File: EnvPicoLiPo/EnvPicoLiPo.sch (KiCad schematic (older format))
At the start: 72 parts, among them J2 SKRKAEE020, J3 2.54mm header 01x20, J4 2.54mm header 01x20, J5 Conn_01x03_Male, U1 LM3671MF 3.3, U2 BQ24072RGT, U3 RP2040, U4 ESP32-PICO-D4, X1 XO 32 12Mhz 3225 seiko

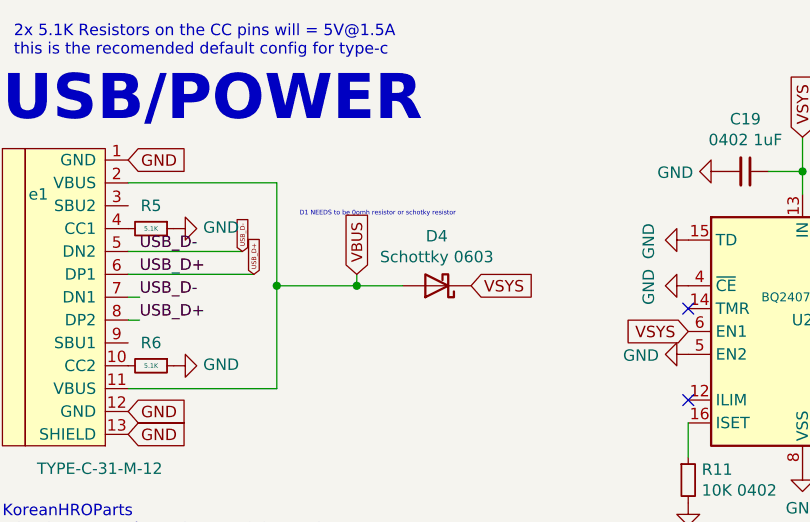
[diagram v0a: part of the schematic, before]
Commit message: Corrected all the via placements so they dont cause issues and removed some redundant parts
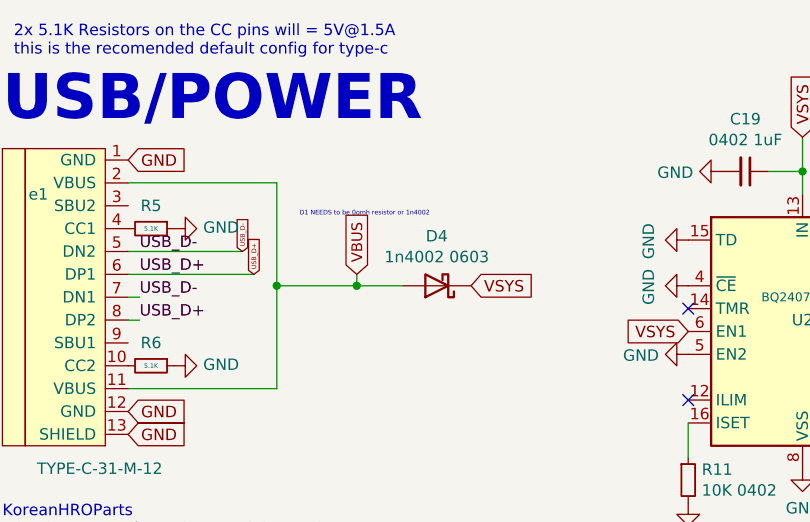
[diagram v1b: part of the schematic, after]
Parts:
- D4: value Schottky 0603 -> 1n4002 0603
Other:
- note added: "D1 NEEDS to be 0omh resistor or 1n4002"
- note removed: "D1 NEEDS to be 0omh resistor or schotky resistor"
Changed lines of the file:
@@
 this is for factory testing\nalways pull this to ground
 Text Notes 1850 1450 0    20   ~ 0
-D1 NEEDS to be 0omh resistor or schotky resistor
+D1 NEEDS to be 0omh resistor or 1n4002
 Connection ~ 6750 1850
 Text GLabel 2100 1700 1    47   Input ~ 0
@@
 P 2450 1750
 F 0 "D4" H 2450 1533 50  0000 C CNN
-F 1 "Schottky 0603" H 2450 1624 50  0000 C CNN
+F 1 "1n4002 0603" H 2450 1624 50  0000 C CNN
 F 2 "Diode_SMD:D_0603_1608Metric" H 2450 1750 50  0001 C CNN
 F 3 "~" H 2450 1750 50  0001 C CNN
